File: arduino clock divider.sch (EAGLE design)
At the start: 36 parts, among them IC1 7805T

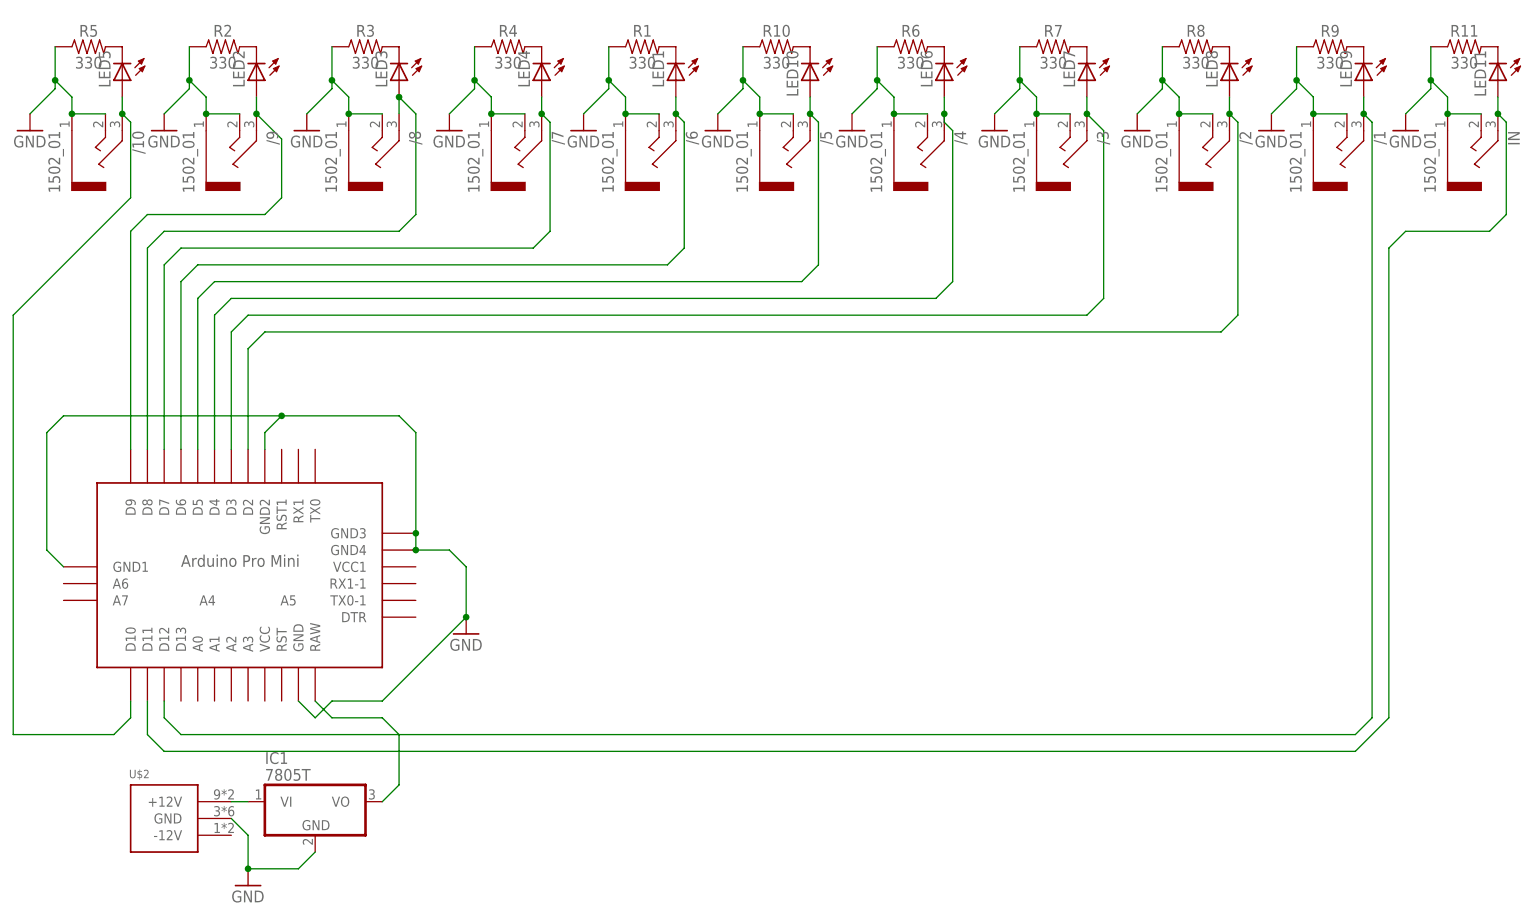
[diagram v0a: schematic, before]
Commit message: A new update
I have added animations.
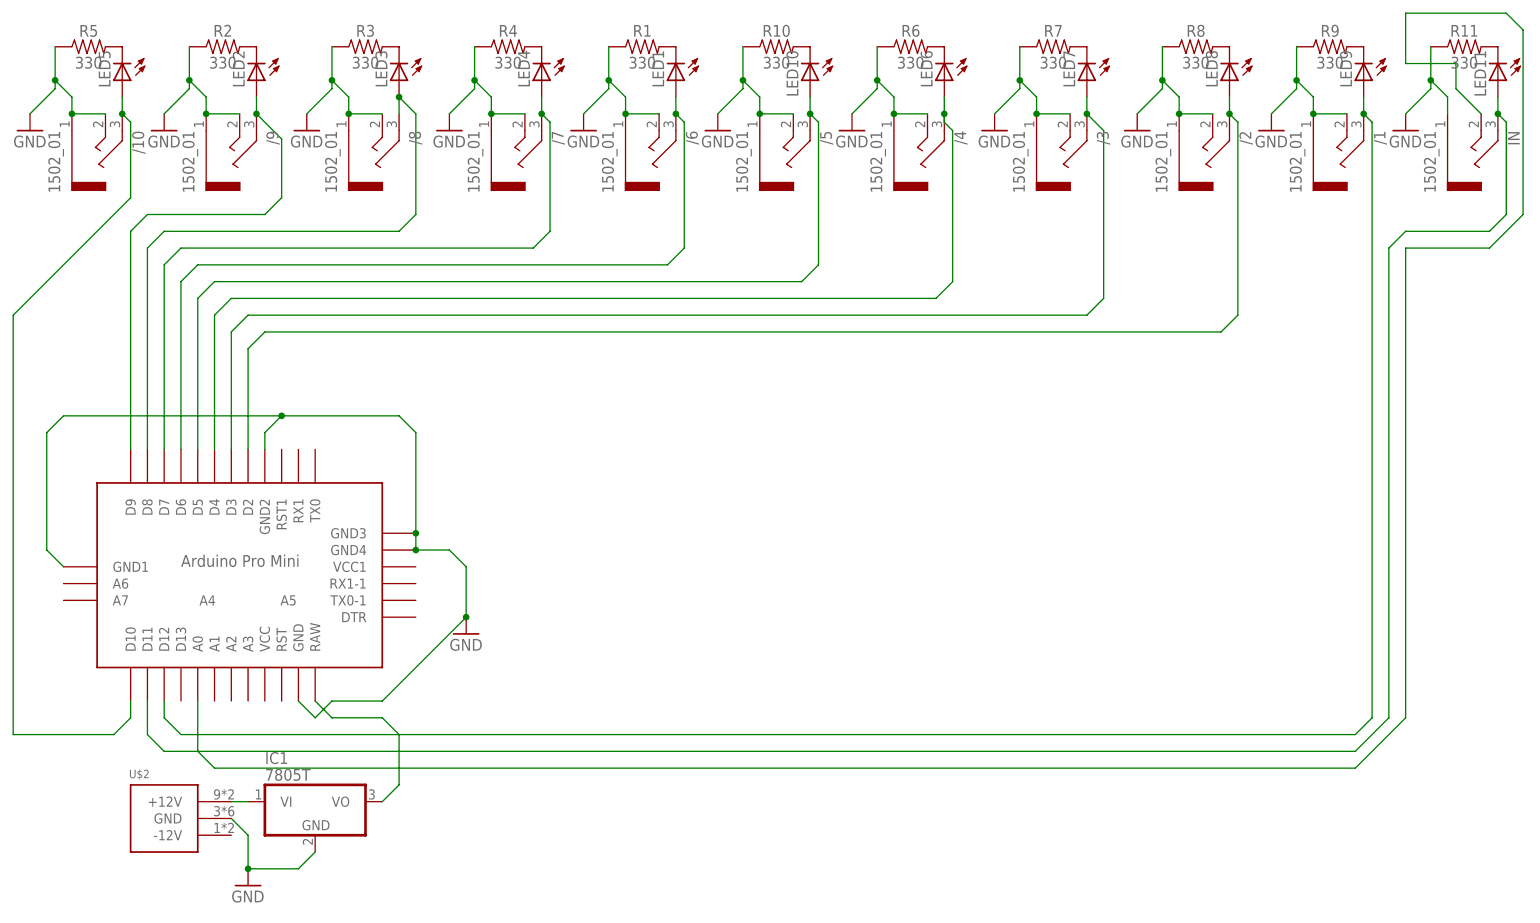
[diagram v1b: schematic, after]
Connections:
- new net N$23: IN.3, U$1.A0
- net GND: no longer IN.3
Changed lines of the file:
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@@
 <setting verticaltext="up"/>
 </settings>
-<grid distance="0.1" unitdist="inch" unit="inch" style="dots" multiple="1" display="yes" altdistance="0.01" altunitdist="inch" altunit="inch"/>
+<grid distance="0.1" unitdist="inch" unit="inch" style="lines" multiple="1" display="no" altdistance="0.01" altunitdist="inch" altunit="inch"/>
 <layers>
 <layer number="1" name="Top" color="4" fill="1" visible="no" active="no"/>
@@
 <pinref part="GND11" gate="1" pin="GND"/>
 <wire x1="208.28" y1="63.5" x2="212.09" y2="67.31" width="0.1524" layer="91"/>
-<pinref part="IN" gate="G$1" pin="3"/>
 <pinref part="IN" gate="G$1" pin="1"/>
-<wire x1="219.71" y1="63.5" x2="214.63" y2="63.5" width="0.1524" layer="91"/>
 <wire x1="214.63" y1="63.5" x2="214.63" y2="66.04" width="0.1524" layer="91"/>
 <wire x1="214.63" y1="66.04" x2="212.09" y2="68.58" width="0.1524" layer="91"/>
-<junction x="214.63" y="63.5"/>
 <pinref part="R11" gate="G$1" pin="1"/>
 <wire x1="212.09" y1="68.58" x2="212.09" y2="73.66" width="0.1524" layer="91"/>
@@
 </segment>
 </net>
+<net name="N$23" class="0">
+<segment>
+<pinref part="U$1" gate="G$1" pin="A0"/>
+<wire x1="25.4" y1="-25.4" x2="25.4" y2="-33.02" width="0.1524" layer="91"/>
+<wire x1="25.4" y1="-33.02" x2="27.94" y2="-35.56" width="0.1524" layer="91"/>
+<wire x1="27.94" y1="-35.56" x2="200.66" y2="-35.56" width="0.1524" layer="91"/>
+<wire x1="200.66" y1="-35.56" x2="208.28" y2="-27.94" width="0.1524" layer="91"/>
+<wire x1="208.28" y1="-27.94" x2="208.28" y2="43.18" width="0.1524" layer="91"/>
+<wire x1="208.28" y1="43.18" x2="220.98" y2="43.18" width="0.1524" layer="91"/>
+<wire x1="220.98" y1="43.18" x2="226.06" y2="48.26" width="0.1524" layer="91"/>
+<wire x1="226.06" y1="48.26" x2="226.06" y2="76.2" width="0.1524" layer="91"/>
+<wire x1="226.06" y1="76.2" x2="223.52" y2="78.74" width="0.1524" layer="91"/>
+<wire x1="223.52" y1="78.74" x2="208.28" y2="78.74" width="0.1524" layer="91"/>
+<wire x1="208.28" y1="78.74" x2="208.28" y2="71.12" width="0.1524" layer="91"/>
+<wire x1="208.28" y1="71.12" x2="215.9" y2="71.12" width="0.1524" layer="91"/>
+<pinref part="IN" gate="G$1" pin="3"/>
+<wire x1="215.9" y1="71.12" x2="215.9" y2="67.31" width="0.1524" layer="91"/>
+<wire x1="215.9" y1="67.31" x2="219.71" y2="63.5" width="0.1524" layer="91"/>
+</segment>
+</net>
